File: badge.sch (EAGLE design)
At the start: 33 parts, among them IC1 MCP1703CB, U1 ESP8266, U2 AT25SF041-SOIC8, Y1 26MHz

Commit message: for ys
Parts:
- removed D2: 1N4148, adafruit:DIODESOD-323F
- removed E1: ANTENNATRACE, SparkFun-RF:ANTENNATRACE
- removed IC1: MCP1703CB, linear:MCP1703CB
- removed JP2: (no value), pinhead:PINHD-1X5
- removed JP3: (no value), pinhead:PINHD-1X4
- removed S1, S2, S3, S4, S5: (no value), gm2:TACT-SW-4P-SMD
- removed Y1: 26MHz, SparkFun-FreqCtrl:CRYSTALCRYSTAL-SMD-5X3-16MHZ
- added ANT1: AN9520, badge:AN9520
- added D3: 1N4148, adafruit:DIODESOD-323F
- added SW1: MK12C02, badge:MK12C02
- added U$1, U$2, U$3, U$4, U$5, U$6: TOUCHSWITCH, badge:TOUCHSWITCH
- added U3: LM317EMP-SOT223, Seeed-OPL-ic:PMIC-LDO-LM317EMP(SOT223)
- added XTAL1: 26MHZ, badge:26MHZ
- C1, C2, C3, C4, C5, C6, C7, C8, C9: device rcl:C-EUC0805 -> resistor:C-EUC0603K
- R1, R2, R3, R4, R5, R6: device rcl:R-US_R0805 -> resistor:R-EU_R0603W
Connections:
- removed net GPIO2: JP3.2, S1.S, S1.S1, U1.GPIO2
- removed net N$7: C7.1, U1.XTAL_IN, Y1.1
- removed net SPI_CLK: JP2.4, LCD1.SCLK, U1.MTMS/SPICLK/GPIO14
- removed net SPI_CS: JP2.5, S4.S, S4.S1, U1.MTDO/SPICS/GPIO15
- removed net SPI_SI: JP2.3, LCD1.SDIN, U1.MTCK/SPID/GPIO13
- removed net SPI_SO: JP2.2, LCD1.D/C, U1.MTDI/SPIQ/GPIO12
- new net ANT: ANT1.P$1, U1.LNA
- new net GPIO12/SPI_SO: LCD1.D/C, U1.MTDI/SPIQ/GPIO12
- new net GPIO13/SPI_SI: LCD1.SDIN, U1.MTCK/SPID/GPIO13
- new net GPIO14/SPI_CLK/SCL: LCD1.SCLK, U1.MTMS/SPICLK/GPIO14
- new net GPIO15/SPI_CS: U$3.P$2, U$4.P$2, U1.MTDO/SPICS/GPIO15
- new net GPIO16: U1.XPD_DCDC/GPIO16
- new net GPIO2/SDA: U$1.P$1, U$3.P$1, U$5.P$1, U1.GPIO2
- net 5V: now also D3.A
- net ADC: no longer JP2.1
- net GND: now also C6.1, C7.1, U3.ADJ; no longer C6.2, C7.2, E1.GND, IC1.GND, S1.P, S1.P1, S2.P, S2.P1, S3.P, S3.P1, S4.P, S4.P1, S5.P, S5.P1
- net GPIO0: now also U$5.P$2, U$6.P$2; no longer JP3.1, S5.S, S5.S1
- net GPIO4: now also U$2.P$1, U$4.P$1, U$6.P$1; no longer JP3.3, S2.S, S2.S1
- net GPIO5: now also U$1.P$2, U$2.P$2; no longer JP3.4, S3.S, S3.S1
- net N$1: now also SW1.P$2, U3.VIN; no longer E1.SIGNAL, U1.LNA
- net N$5: now also D3.C, SW1.P$1; no longer IC1.VI
- net N$6: now also C6.2, U1.XTAL_OUT, XTAL1.P$1; no longer D2.C, U1.XPD_DCDC/GPIO16
- net N$8: now also C7.2, U1.XTAL_IN, XTAL1.P$2; no longer C6.1, U1.XTAL_OUT, Y1.2
- net RESET: no longer D2.A
- net VCC: now also U3.VOUT; no longer IC1.VO
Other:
- note removed: "1, 2, 3, 4 Up, Down, Left, Right"
- note removed: "ADC GPIO12-15"
- note removed: "GPIO0,2,4,5"
- moved on the sheet: B1, B2, C3, C4, C5, C6, C7, C8, C9, D1, JP1, LCD1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

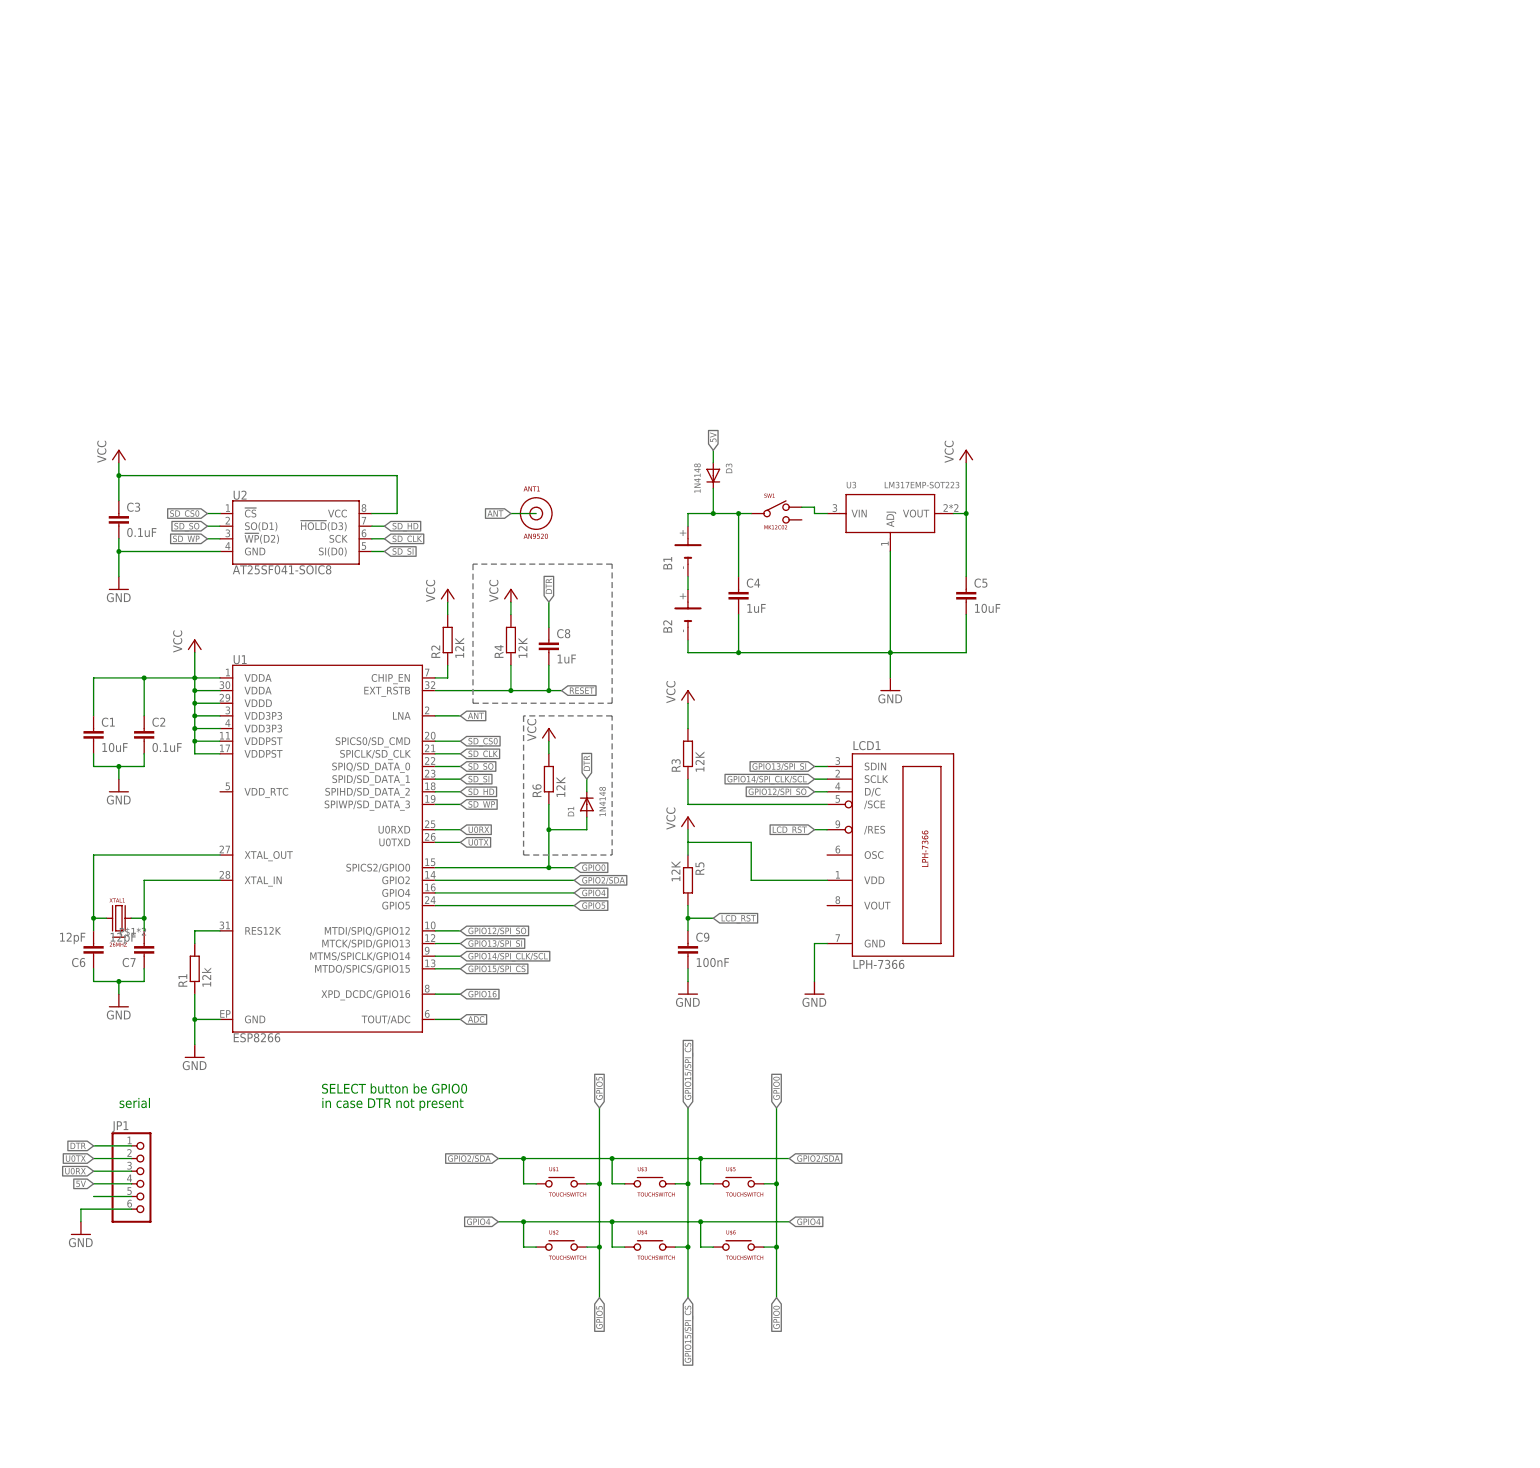
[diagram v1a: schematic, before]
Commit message: switching over to ESP-12e/f
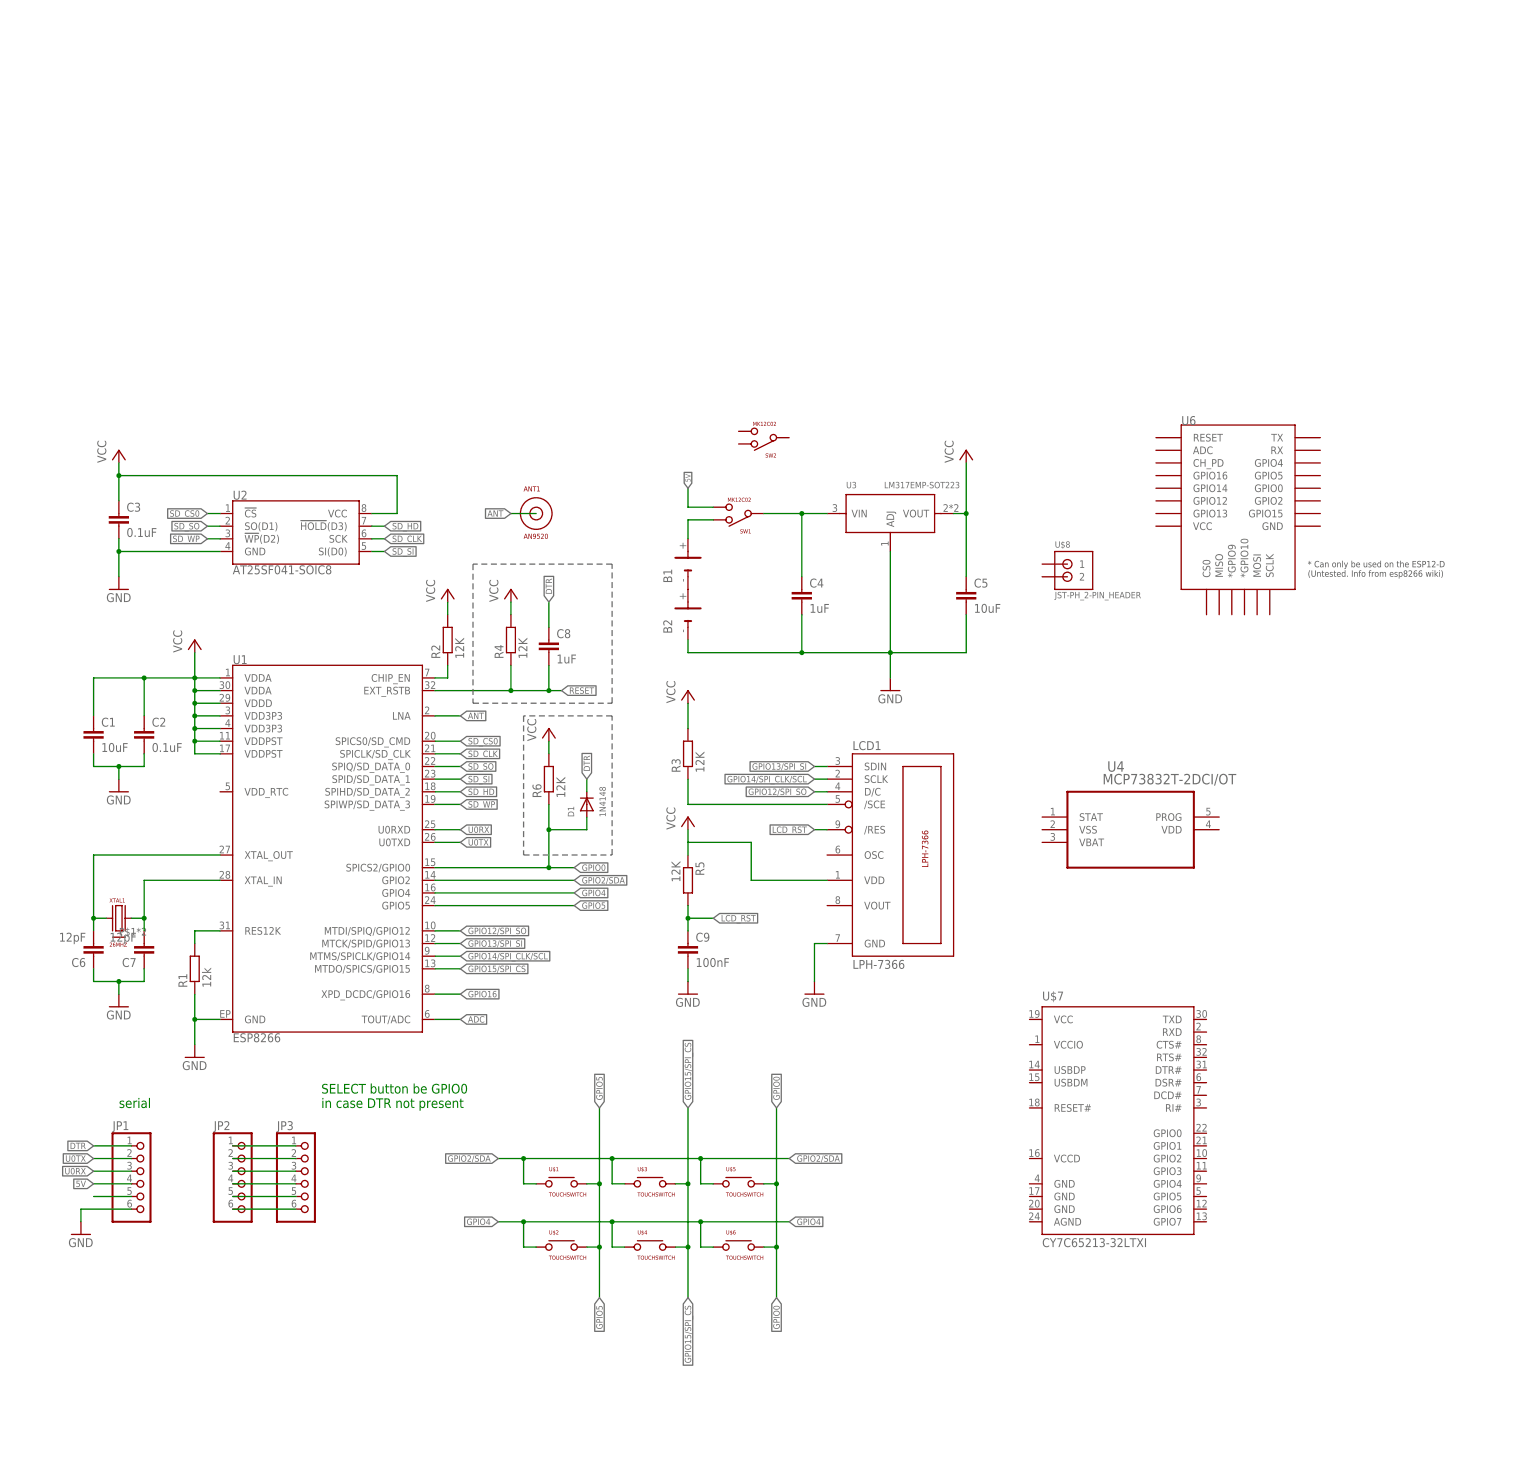
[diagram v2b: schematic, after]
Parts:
- removed D3: 1N4148, adafruit:DIODESOD-323F
- added JP2, JP3: (no value), pinhead:PINHD-1X6
- added SW2: MK12C02, badge:MK12C02
- added U$7: CY7C65213-32LTXI, cypress_usb-serial:CY7C65213-32LTXI
- added U$8: JST-PH_2-PIN_HEADER, SRG:JST-PH_2-PIN_HEADER
- added U4: MCP73832T-2DCI/OT, Microchip_By_element14_Batch_1:MCP73832T-2DCI/OT
- added U6: (no value), esp8266modules:ESP12ESMD
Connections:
- new net N$10: JP2.2, JP3.2
- new net N$11: JP2.3, JP3.3
- new net N$12: JP2.4, JP3.4
- new net N$13: JP2.5, JP3.5
- new net N$14: JP2.6, JP3.6
- new net N$7: JP2.1, JP3.1
- net 5V: now also SW1.P$3; no longer D3.A
- net N$1: now also C4.1, SW1.P$1; no longer SW1.P$2
- net N$5: now also SW1.P$2; no longer C4.1, D3.C, SW1.P$1
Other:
- moved on the sheet: B1, C4, SW1
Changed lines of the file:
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@@
 <part name="P+9" library="supply1" deviceset="VCC" device=""/>
 <part name="U3" library="Seeed-OPL-ic" deviceset="PMIC-LDO-LM317EMP(SOT223)" device="" value="LM317EMP-SOT223"/>
-<part name="D3" library="adafruit" deviceset="DIODE" device="SOD-323F" value="1N4148"/>
 <part name="XTAL1" library="badge" deviceset="26MHZ" device=""/>
 <part name="U$1" library="badge" deviceset="TOUCHSWITCH" device=""/>
@@
 <part name="SW1" library="badge" deviceset="MK12C02" device=""/>
 <part name="ANT1" library="badge" deviceset="AN9520" device=""/>
+<part name="JP2" library="pinhead" deviceset="PINHD-1X6" device=""/>
+<part name="JP3" library="pinhead" deviceset="PINHD-1X6" device=""/>
+<part name="SW2" library="badge" deviceset="MK12C02" device=""/>
+<part name="U$7" library="cypress_usb-serial" deviceset="CY7C65213-32LTXI*" device=""/>
+<part name="U4" library="Microchip_By_element14_Batch_1" deviceset="MCP73832T-2DCI/OT" device=""/>
+<part name="U6" library="esp8266modules" deviceset="ESP12E" device="SMD"/>
+<part name="U$8" library="SRG" deviceset="JST-PH_2-PIN_HEADER" device=""/>
 </parts>
 <sheets>
@@
 <instance part="P+4" gate="VCC" x="134.62" y="76.2"/>
 <instance part="R3" gate="G$1" x="134.62" y="63.5" rot="R90"/>
-<instance part="C4" gate="G$1" x="144.78" y="96.52"/>
+<instance part="C4" gate="G$1" x="157.48" y="96.52"/>
 <instance part="C5" gate="G$1" x="190.5" y="96.52"/>
 <instance part="P+5" gate="VCC" x="190.5" y="124.46"/>
@@
 <instance part="JP1" gate="A" x="25.4" y="-22.86"/>
 <instance part="GND9" gate="1" x="12.7" y="-33.02"/>
-<instance part="B1" gate="G$1" x="134.62" y="104.14" rot="R90"/>
+<instance part="B1" gate="G$1" x="134.62" y="101.6" rot="R90"/>
 <instance part="B2" gate="G$1" x="134.62" y="91.44" rot="R90"/>
 <instance part="C9" gate="G$1" x="134.62" y="25.4"/>
@@
 <instance part="P+9" gate="VCC" x="99.06" y="96.52"/>
 <instance part="U3" gate="G$1" x="175.26" y="111.76"/>
-<instance part="D3" gate="G$1" x="139.7" y="119.38" rot="R270"/>
 <instance part="XTAL1" gate="G$1" x="20.32" y="30.48"/>
 <instance part="U$1" gate="G$1" x="109.22" y="-22.86"/>
@@
 <instance part="U$5" gate="G$1" x="144.78" y="-22.86"/>
 <instance part="U$6" gate="G$1" x="144.78" y="-35.56"/>
-<instance part="SW1" gate="G$1" x="152.4" y="111.76"/>
+<instance part="SW1" gate="G$1" x="144.78" y="111.76" rot="R180"/>
 <instance part="ANT1" gate="G$1" x="104.14" y="111.76"/>
+<instance part="JP2" gate="A" x="45.72" y="-22.86"/>
+<instance part="JP3" gate="A" x="58.42" y="-22.86"/>
+<instance part="SW2" gate="G$1" x="149.86" y="127" rot="R180"/>
+<instance part="U$7" gate="G$1" x="220.98" y="-10.16"/>
+<instance part="U4" gate="A" x="223.52" y="50.8"/>
+<instance part="U6" gate="G$1" x="246.38" y="119.38"/>
+<instance part="U$8" gate="G$1" x="213.36" y="99.06"/>
 </instances>
 <busses>
@@
 <segment>
 <pinref part="C4" gate="G$1" pin="2"/>
-<wire x1="144.78" y1="91.44" x2="144.78" y2="83.82" width="0.1524" layer="91"/>
+<wire x1="157.48" y1="91.44" x2="157.48" y2="83.82" width="0.1524" layer="91"/>
 <pinref part="C5" gate="G$1" pin="2"/>
 <wire x1="190.5" y1="91.44" x2="190.5" y2="83.82" width="0.1524" layer="91"/>
@@
 <pinref part="B2" gate="G$1" pin="-"/>
 <wire x1="134.62" y1="86.36" x2="134.62" y2="83.82" width="0.1524" layer="91"/>
-<wire x1="134.62" y1="83.82" x2="144.78" y2="83.82" width="0.1524" layer="91"/>
-<wire x1="144.78" y1="83.82" x2="175.26" y2="83.82" width="0.1524" layer="91"/>
-<junction x="144.78" y="83.82"/>
+<wire x1="134.62" y1="83.82" x2="157.48" y2="83.82" width="0.1524" layer="91"/>
+<wire x1="157.48" y1="83.82" x2="175.26" y2="83.82" width="0.1524" layer="91"/>
+<junction x="157.48" y="83.82"/>
 <pinref part="U3" gate="G$1" pin="ADJ"/>
 <wire x1="175.26" y1="83.82" x2="175.26" y2="104.14" width="0.1524" layer="91"/>
@@
 <wire x1="40.64" y1="106.68" x2="38.1" y2="106.68" width="0.1524" layer="91"/>
 <label x="38.1" y="106.68" size="1.27" layer="95" rot="MR0" xref="yes"/>
-</segment>
-</net>
-<net name="N$5" class="0">
-<segment>
-<pinref part="C4" gate="G$1" pin="1"/>
-<wire x1="144.78" y1="111.76" x2="144.78" y2="99.06" width="0.1524" layer="91"/>
-<pinref part="B1" gate="G$1" pin="+"/>
-<wire x1="134.62" y1="109.22" x2="134.62" y2="111.76" width="0.1524" layer="91"/>
-<wire x1="134.62" y1="111.76" x2="139.7" y2="111.76" width="0.1524" layer="91"/>
-<pinref part="D3" gate="G$1" pin="C"/>
-<wire x1="139.7" y1="111.76" x2="144.78" y2="111.76" width="0.1524" layer="91"/>
-<wire x1="139.7" y1="116.84" x2="139.7" y2="111.76" width="0.1524" layer="91"/>
-<junction x="139.7" y="111.76"/>
-<pinref part="SW1" gate="G$1" pin="P$1"/>
-<wire x1="144.78" y1="111.76" x2="147.32" y2="111.76" width="0.1524" layer="91"/>
-<junction x="144.78" y="111.76"/>
 </segment>
 </net>
@@
 </segment>
 <segment>
-<pinref part="D3" gate="G$1" pin="A"/>
-<wire x1="139.7" y1="121.92" x2="139.7" y2="124.46" width="0.1524" layer="91"/>
-<label x="139.7" y="124.46" size="1.27" layer="95" rot="R90" xref="yes"/>
+<pinref part="SW1" gate="G$1" pin="P$3"/>
+<wire x1="139.7" y1="113.03" x2="134.62" y2="113.03" width="0.1524" layer="91"/>
+<wire x1="134.62" y1="113.03" x2="134.62" y2="116.84" width="0.1524" layer="91"/>
+<label x="134.62" y="116.84" size="1.016" layer="95" rot="R90" xref="yes"/>
 </segment>
 </net>
@@
 <pinref part="B1" gate="G$1" pin="-"/>
 <pinref part="B2" gate="G$1" pin="+"/>
-<wire x1="134.62" y1="99.06" x2="134.62" y2="96.52" width="0.1524" layer="91"/>
 </segment>
 </net>
@@
 <net name="N$1" class="0">
 <segment>
+<pinref part="U3" gate="G$1" pin="VIN"/>
+<pinref part="SW1" gate="G$1" pin="P$1"/>
+<wire x1="162.56" y1="111.76" x2="157.48" y2="111.76" width="0.1524" layer="91"/>
+<pinref part="C4" gate="G$1" pin="1"/>
+<wire x1="157.48" y1="111.76" x2="149.86" y2="111.76" width="0.1524" layer="91"/>
+<wire x1="157.48" y1="99.06" x2="157.48" y2="111.76" width="0.1524" layer="91"/>
+<junction x="157.48" y="111.76"/>
+</segment>
+</net>
+<net name="N$7" class="0">
+<segment>
+<pinref part="JP2" gate="A" pin="1"/>
+<pinref part="JP3" gate="A" pin="1"/>
+<wire x1="43.18" y1="-15.24" x2="55.88" y2="-15.24" width="0.1524" layer="91"/>
+</segment>
+</net>
+<net name="N$10" class="0">
+<segment>
+<pinref part="JP3" gate="A" pin="2"/>
+<pinref part="JP2" gate="A" pin="2"/>
+<wire x1="55.88" y1="-17.78" x2="43.18" y2="-17.78" width="0.1524" layer="91"/>
+</segment>
+</net>
+<net name="N$11" class="0">
+<segment>
+<pinref part="JP2" gate="A" pin="3"/>
+<pinref part="JP3" gate="A" pin="3"/>
+<wire x1="43.18" y1="-20.32" x2="55.88" y2="-20.32" width="0.1524" layer="91"/>
+</segment>
+</net>
+<net name="N$12" class="0">
+<segment>
+<pinref part="JP3" gate="A" pin="4"/>
+<pinref part="JP2" gate="A" pin="4"/>
+<wire x1="55.88" y1="-22.86" x2="43.18" y2="-22.86" width="0.1524" layer="91"/>
+</segment>
+</net>
+<net name="N$13" class="0">
+<segment>
+<pinref part="JP2" gate="A" pin="5"/>
+<pinref part="JP3" gate="A" pin="5"/>
+<wire x1="43.18" y1="-25.4" x2="55.88" y2="-25.4" width="0.1524" layer="91"/>
+</segment>
+</net>
+<net name="N$14" class="0">
+<segment>
+<pinref part="JP3" gate="A" pin="6"/>
+<pinref part="JP2" gate="A" pin="6"/>
+<wire x1="55.88" y1="-27.94" x2="43.18" y2="-27.94" width="0.1524" layer="91"/>
+</segment>
+</net>
+<net name="N$5" class="0">
+<segment>
+<pinref part="B1" gate="G$1" pin="+"/>
+<wire x1="134.62" y1="106.68" x2="134.62" y2="110.49" width="0.1524" layer="91"/>
 <pinref part="SW1" gate="G$1" pin="P$2"/>
-<wire x1="157.48" y1="113.03" x2="160.02" y2="113.03" width="0.1524" layer="91"/>
-<wire x1="160.02" y1="113.03" x2="160.02" y2="111.76" width="0.1524" layer="91"/>
-<pinref part="U3" gate="G$1" pin="VIN"/>
-<wire x1="160.02" y1="111.76" x2="162.56" y2="111.76" width="0.1524" layer="91"/>
-</segment>
-</net>
+<wire x1="134.62" y1="110.49" x2="139.7" y2="110.49" width="0.1524" layer="91"/>
+</segment>
+</net>
